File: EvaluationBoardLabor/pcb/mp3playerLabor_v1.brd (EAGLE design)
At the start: 99 x 98.7 mm, 25 parts, among them IC1 4050N, Q1 12MHz, X1 FPS009-3000, X2 1503_09

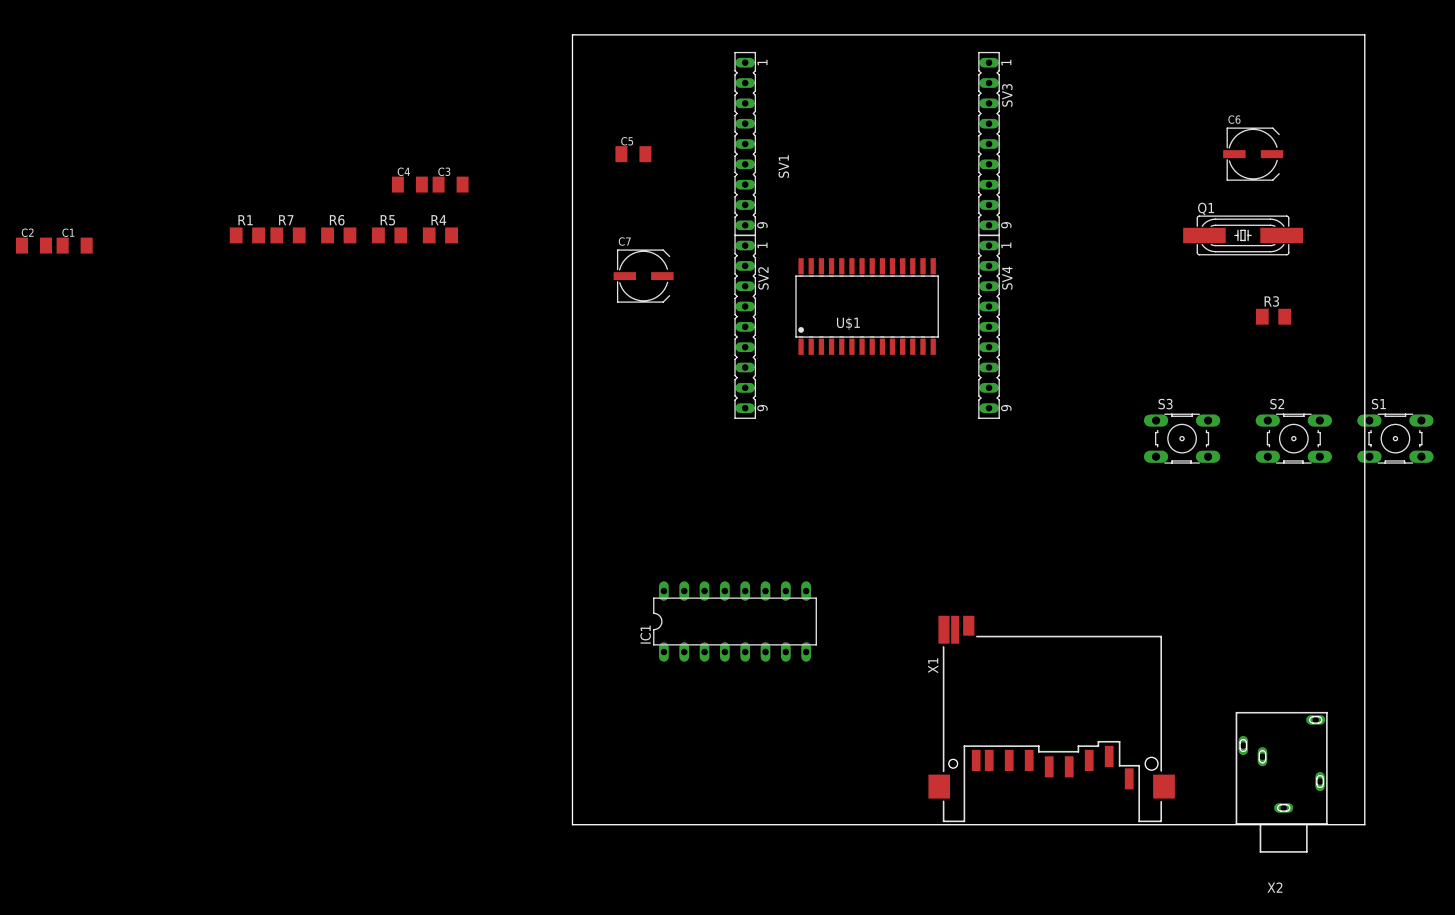
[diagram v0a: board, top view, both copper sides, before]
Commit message: update schematic
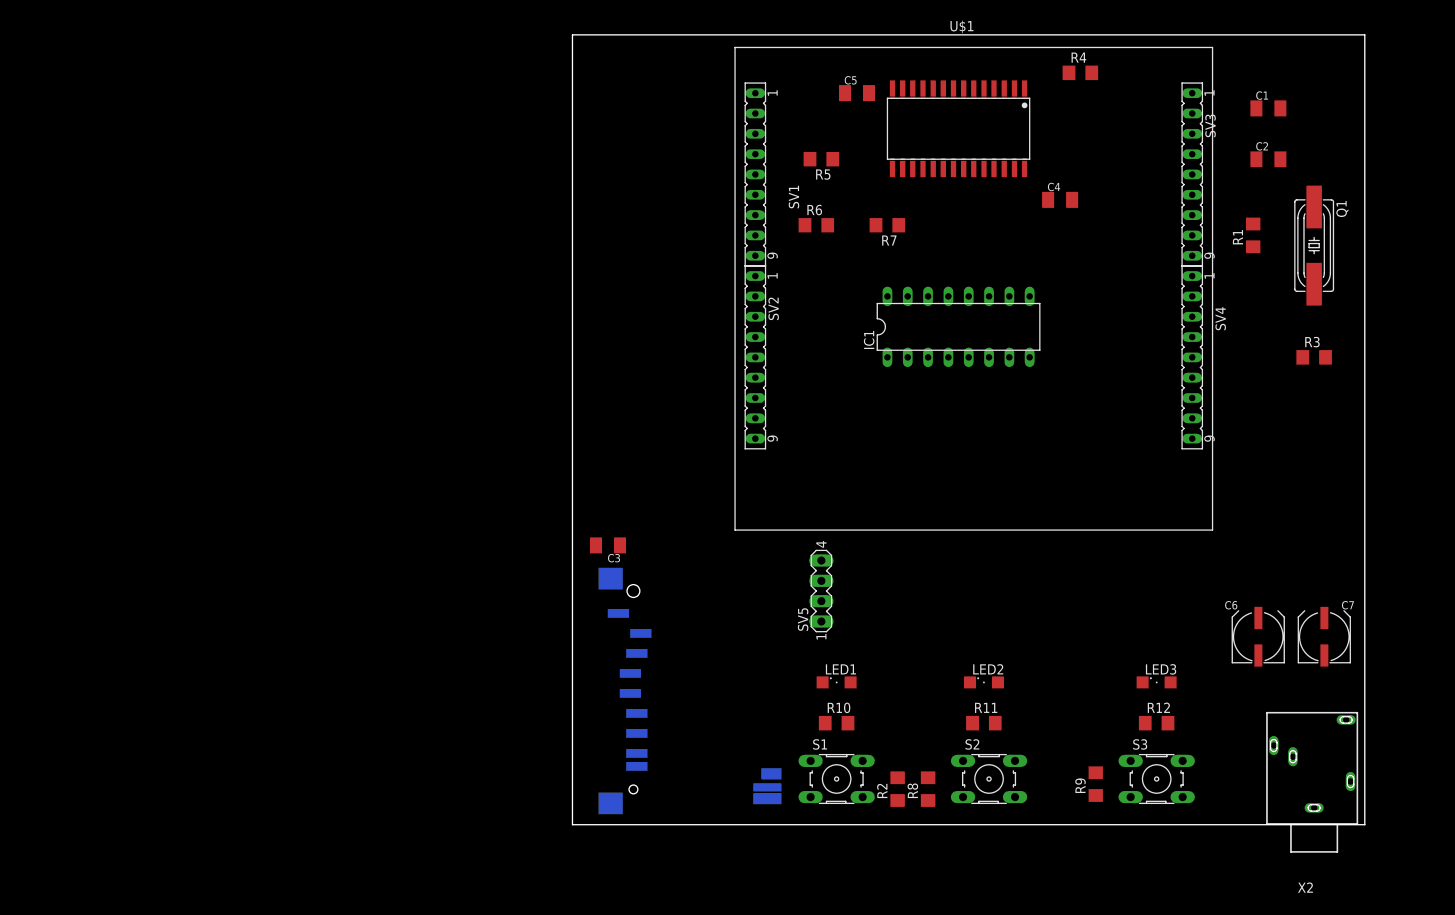
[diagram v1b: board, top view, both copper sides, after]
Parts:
- added LED1, LED2, LED3: (no value), led:SML1206
- added R10, R11, R12: 390, rcl:R1206
- added R2, R8, R9: 100k, rcl:R1206
- added SV5: (no value), con-lstb:MA04-1
- R1, R3, R4, R5, R6, R7: device rcl:M1206 -> rcl:R1206
- X1: value FPS009-3000 -> SD-Card holder
- moved C2 154.7 mm to (87.0, 83.2)
- moved C1 150.2 mm to (87.0, 89.5)
- moved R1 125.7 mm to (85.1, 73.7), turned to 90 degrees
- moved C7 96.3 mm to (94.0, 23.5), turned to 90 degrees
- moved R4 82.5 mm to (63.5, 94.0)
- moved S1 81.8 mm to (33.0, 5.71)
- moved C4 81.3 mm to (61.0, 78.1)
- moved R7 74.9 mm to (39.4, 74.9), turned to 180 degrees
- moved X1 68.3 mm to (7.62, 29.2), flipped to the bottom, turned to 0 degrees
- moved C6 60.3 mm to (85.7, 23.5), turned to 90 degrees
- moved R6 59.7 mm to (30.5, 74.9)
- moved S2 57.1 mm to (52.1, 5.71)
- moved R5 54.8 mm to (31.1, 83.2), turned to 180 degrees
- moved C3 49.2 mm to (4.45, 34.9), turned to 180 degrees
- moved IC1 46.2 mm to (48.3, 62.2)
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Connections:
- removed net AREF: SV3.3
- removed net N$1: U$1.12, X1.5
- removed net N$15: U$1.1
- removed net N$17: R7.1, U$1.26
- removed net N$2: U$1.14, X1.7
- removed net N$3: U$1.13, X1.2
- removed net VDD: IC1.1
- new net CSCARD: IC1.6, X1.1
- new net MOSI: IC1.4, U$1.13, X1.2
- new net SCK: IC1.2, U$1.12, X1.5
- new net XCS: IC1.10, U$1.11
- new net XDCS: IC1.12, U$1.4
- new net XRESET: IC1.15, R7.1, U$1.26
- net +3V3: now also C5.1, IC1.1, SV3.3
- net +5V: now also S1.1, S2.1, S3.1, SV5.2
- net GND: now also C5.2, R10.2, R11.2, R12.2, R2.2, R8.2, R9.2, SV5.1
- net N$4: now also LED1.C, R10.1; no longer U$1.11
- net N$5: now also LED2.C, R11.1; no longer X1.1
- net N$7: now also LED3.C, R12.1; no longer U$1.4
- net PB1: now also IC1.7
- net PB2: now also IC1.9
- net PB3: now also IC1.5
- net PB4: now also U$1.14, X1.7
- net PB5: now also IC1.3
- net PC0: now also IC1.11
- net PC1: now also U$1.1
- net PC3: now also IC1.14
- net PC4: now also SV5.4
- net PC5: now also SV5.3
- net PD2: now also R2.1, S1.3
- net PD3: now also R8.1, S2.3
- net PD4: now also R9.1, S3.3
- net PD5: now also LED1.A
- net PD6: now also LED2.A
- net PD7: now also LED3.A

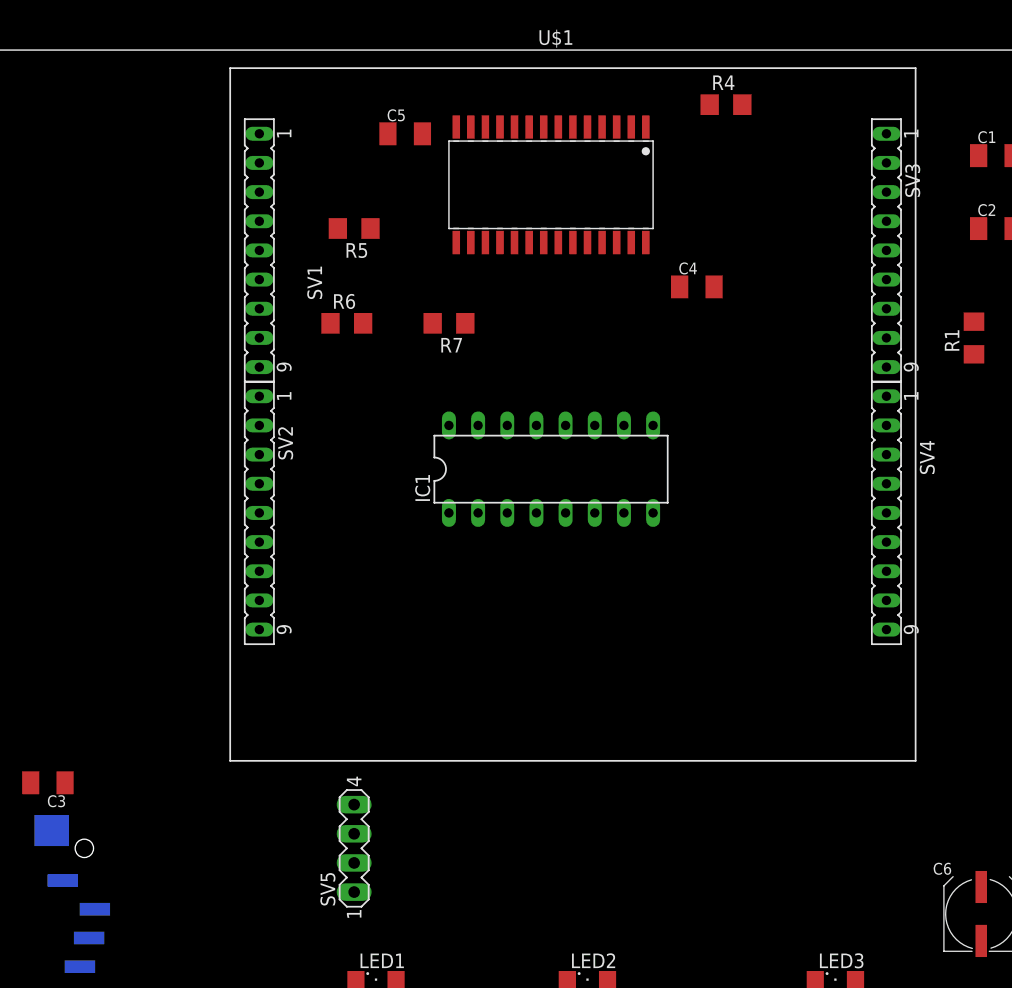
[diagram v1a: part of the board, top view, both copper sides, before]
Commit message: DisplayTest added
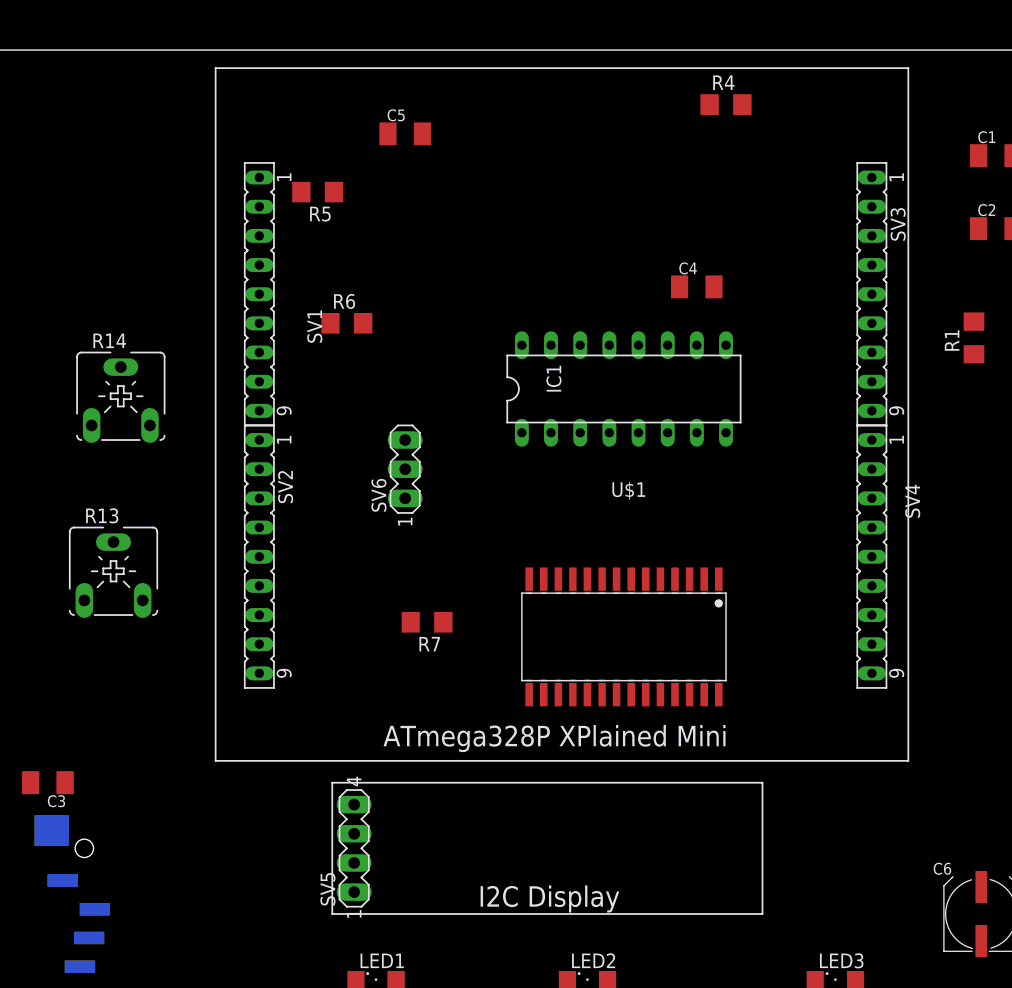
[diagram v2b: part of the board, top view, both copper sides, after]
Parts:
- added R13, R14: (no value), pot:CA6V
- added SV6: (no value), con-lstb:MA03-1
- moved U$1 39.9 mm to (55.9, 47.6)
- moved R7 26.1 mm to (37.5, 48.9)
- moved IC1 9.44 mm to (54.6, 69.2)
- moved R5 4.49 mm to (27.9, 86.4)
- moved SV3 4.02 mm to (76.2, 77.5)
- moved SV4 4.02 mm to (76.2, 54.6)
- moved SV1 3.81 mm to (22.9, 77.5)
- moved SV2 3.81 mm to (22.9, 54.6)
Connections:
- new net ADC6: R13.S, SV6.2
- new net ADC7: R14.S, SV6.1
- net +5V: now also R13.E, R14.E
- net GND: now also R13.A, R14.A
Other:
- board text added: "ATmega328P XPlained Mini"
- board text added: "I2C Display"

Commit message: update pcb
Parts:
- added R15, R16: 100k, rcl:R1206
- moved R5 52.4 mm to (45.1, 36.8), turned to 270 degrees
- moved C4 51.7 mm to (70.5, 27.3), turned to 90 degrees
- moved C1 50.3 mm to (83.8, 39.4)
- moved R4 43.3 mm to (66.0, 50.8), turned to 90 degrees
- moved R6 42.3 mm to (48.9, 36.8), turned to 270 degrees
- moved Q1 39.6 mm to (55.2, 59.7), turned to 0 degrees
- moved C2 33.3 mm to (82.5, 50.2)
- moved R7 28.8 mm to (59.1, 29.8)
- moved R1 28.6 mm to (85.7, 45.1), turned to 270 degrees
- moved X1 24.8 mm to (7.62, 4.45), flipped to the top, turned to 180 degrees
- moved C5 22.3 mm to (57.1, 85.7)
- moved C3 19.1 mm to (3.17, 15.9), turned to 90 degrees
- moved R13 18.4 mm to (9.53, 71.8)
- moved R8 17.5 mm to (61.0, 10.2)
- moved R14 14.0 mm to (9.53, 54.6)
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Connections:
- net +5V: now also R15.1, R16.1
- net PC4: now also R16.2
- net PC5: now also R15.2
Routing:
- net +5V: track 0.00 -> 195.3 mm, vias 0 -> 2
- net PD5: track 0.00 -> 78.2 mm, vias 0 -> 2
- net GND: track 0.00 -> 74.2 mm, vias 0 -> 2
- net +3V3: track 0.00 -> 67.1 mm
- net PD6: track 0.00 -> 62.7 mm, vias 0 -> 2
- net N$20: track 0.00 -> 51.5 mm
- net N$19: track 0.00 -> 49.0 mm
- net PD7: track 0.00 -> 47.5 mm, vias 0 -> 1
- net ADC6: track 0.00 -> 37.4 mm, vias 0 -> 1
- net PC4: track 0.00 -> 30.6 mm
- net ADC7: track 0.00 -> 28.9 mm
- net N$23: track 0.00 -> 26.4 mm
- net PC5: track 0.00 -> 24.9 mm
- net PB5: track 0.00 -> 23.9 mm
- net PB3: track 0.00 -> 23.9 mm
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
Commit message: pcb finished, 1st version
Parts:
- R13, R14: value (none) -> 10k
- moved R3 58.8 mm to (34.9, 47.6), turned to 270 degrees
- moved C1 41.9 mm to (41.9, 39.4)
- moved C4 39.3 mm to (61.0, 65.4), turned to 180 degrees
- moved R1 37.9 mm to (48.3, 39.4), turned to 180 degrees
- moved R7 35.9 mm to (34.3, 55.9)
- moved R4 35.7 mm to (30.5, 47.6), turned to 270 degrees
- moved C2 29.4 mm to (55.2, 39.4), turned to 180 degrees
- moved R5 28.9 mm to (61.0, 61.0), turned to 0 degrees
- moved X2 28.0 mm to (99.1, 27.3), turned to 270 degrees
- moved R6 24.2 mm to (61.0, 57.8), turned to 0 degrees
- moved C5 21.9 mm to (35.6, 81.9), turned to 90 degrees
- moved Q1 16.8 mm to (48.3, 44.5), turned to 180 degrees
- moved C6 16.5 mm to (92.7, 39.4)
- moved C7 16.5 mm to (85.1, 39.4)
- moved U$1 14.5 mm to (47.0, 59.1), turned to 0 degrees
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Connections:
- net PC4: no longer SV3.2
- net PC5: no longer SV3.1
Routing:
- net GND: track 74.2 -> 493.7 mm
- net +3V3: track 67.1 -> 235.6 mm, vias 0 -> 5
- net PB4: track 0.00 -> 125.6 mm, vias 0 -> 2
- net MOSI: track 0.00 -> 110.9 mm, vias 0 -> 2
- net SCK: track 0.00 -> 106.6 mm, vias 0 -> 2
- net CSCARD: track 0.00 -> 106.6 mm, vias 0 -> 1
- net PD2: track 4.68 -> 89.7 mm, vias 0 -> 1
- net PD3: track 5.95 -> 74.2 mm, vias 0 -> 1
- net PC0: track 0.00 -> 66.8 mm
- net PC3: track 0.00 -> 63.5 mm
- net PD4: track 14.1 -> 67.7 mm
- net XDCS: track 0.00 -> 41.9 mm, vias 0 -> 1
- net XRESET: track 0.00 -> 37.2 mm, vias 0 -> 1
- net XCS: track 0.00 -> 33.8 mm, vias 0 -> 1
- net PB1: track 0.00 -> 32.9 mm, vias 0 -> 1
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
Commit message: pcb finished and order sent to jlcpcb
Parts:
- Q1: value 12MHz -> 12,288 MHz
- X1: value SD-Card holder -> SD-Card
- moved C6 1.27 mm to (94.0, 39.4)
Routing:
- net N$22: track 31.3 -> 30.0 mm
- net N$20: track 81.5 -> 82.0 mm
- added copper zone on layer 1, net GND
- added copper zone on layer 16, net GND
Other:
- board text added: "+5V"
- board text added: "0V"
- board text added: "ADC 6"
- board text added: "ADC 7"
- board text added: "ADC6"
- board text added: "ADC7"
- board text added: "GND"
- board text added: "HTL Saalfelden"
- board text added: "MP3-Player Board"
- board text added: "SCL"
- board text added: "SDA"
- board text added: "V1.0 - 11/2019"
